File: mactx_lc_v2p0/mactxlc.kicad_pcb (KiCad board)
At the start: 2 copper layers, 54.8 x 21.7 mm, 8 parts, among them J1 Conn_02x12_Top_Bottom, J2 Conn_01x07, SW1 SW_DIP_x01, U1 MAX660

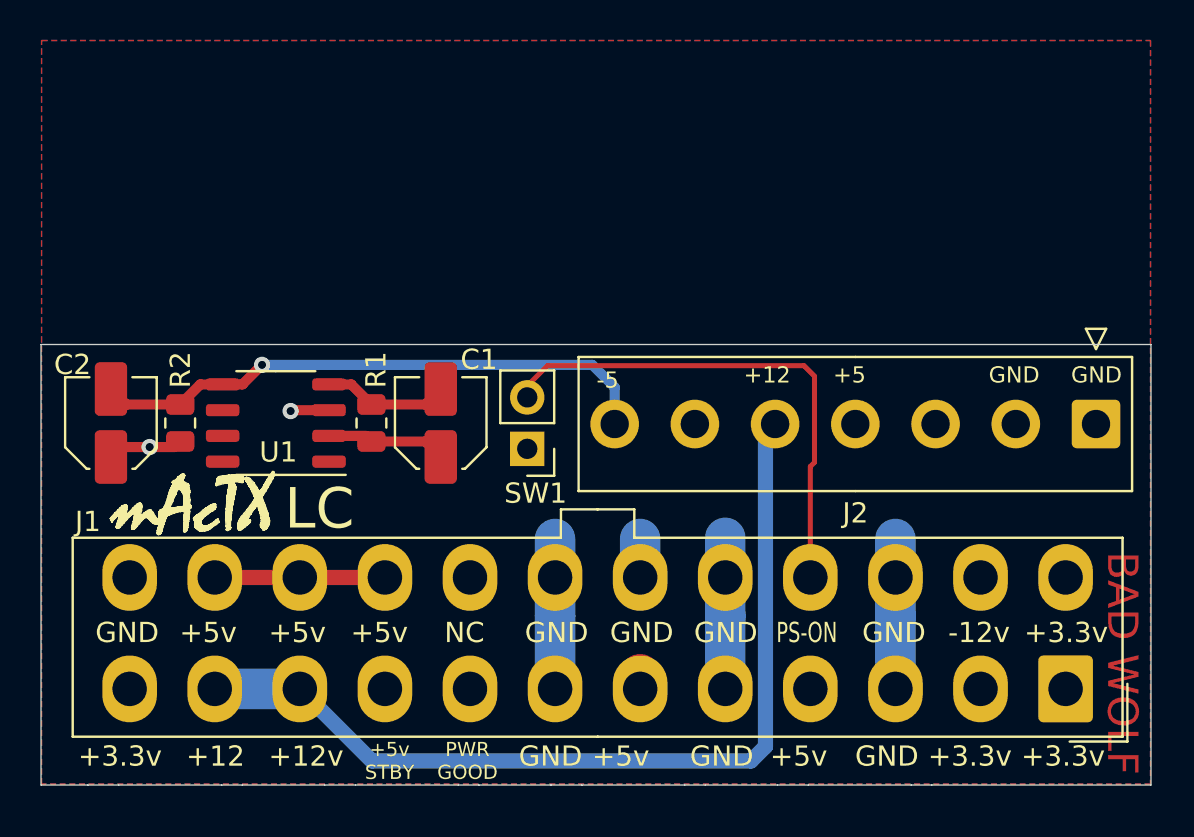
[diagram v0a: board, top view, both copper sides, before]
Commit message: Fixed LC power connector and resistor part number
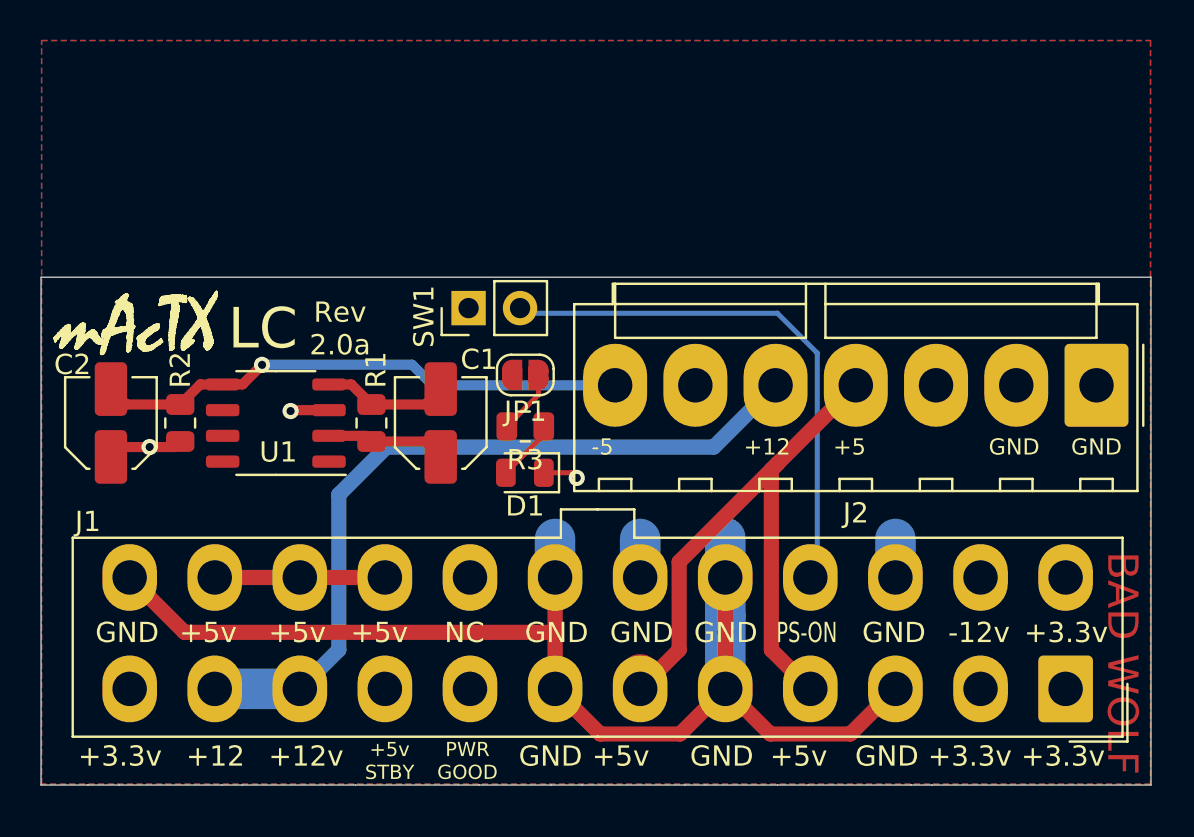
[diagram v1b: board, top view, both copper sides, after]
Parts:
- added D1: LED_Small, LED_SMD:LED_0805_2012Metric, F.Cu at (228.8, 54.4)
- added JP1: SolderJumper_2_Open, Jumper:SolderJumper-2_P1.3mm_Open_RoundedPad1.0x1.5mm, F.Cu at (228.9, 49.5)
- added R3: 10k, Resistor_SMD:R_0805_2012Metric, F.Cu at (228.9, 52.1)
- J2: footprint Connector_TE-Connectivity:TE_826576-7_1x07_P3.96mm_Vertical -> Connector_Molex:Molex_KK-396_A-41791-0007_1x07_P3.96mm_Vertical
- moved SW1 7.53 mm to (226.1, 46.2), turned to 90 degrees
- moved J2 1.91 mm to (257.0, 50.0)
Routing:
- net /GND: track 29.2 -> 73.6 mm, vias 2 -> 3
- net /+5: track 9.12 -> 40.6 mm
- net /+12: track 44.4 -> 38.4 mm
- net Net-(JP1-Pad1): track 0.00 -> 3.19 mm
- net Net-(D1-Pad2): track 0.00 -> 3.06 mm
- net Net-(J1-Pad16): track 24.8 -> 26.7 mm
- net /-5: track 28.3 -> 26.4 mm
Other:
- board size 54.8 x 21.7 mm -> 54.8 x 25.1 mm
- board text added: "Rev 2.0a"
- board text removed: "Rev2.0"
